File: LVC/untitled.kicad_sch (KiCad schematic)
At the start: 3 parts

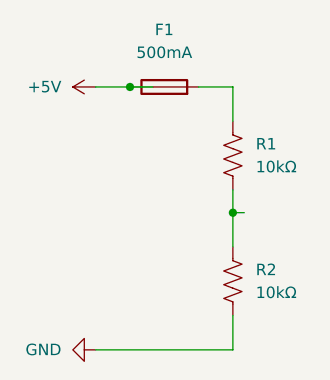
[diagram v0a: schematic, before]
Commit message: Refining Schematics
Refined the visuals of all the schematics to remove values from components. Also removed a redundant schematic.
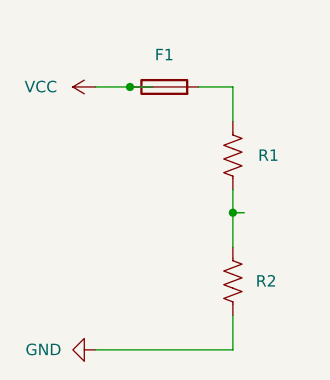
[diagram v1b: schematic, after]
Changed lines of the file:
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@@
 		(in_pos_files yes)
 		(dnp no)
-		(fields_autoplaced yes)
 		(property "Reference" "F1"
-			(at 143.51 64.77 90)
+			(at 143.51 67.564 90)
 			(show_name no)
 			(do_not_autoplace no)
@@
 		(property "Value" "500mA"
 			(at 143.51 67.31 90)
+			(hide yes)
 			(show_name no)
 			(do_not_autoplace no)
@@
 		(in_pos_files yes)
 		(dnp no)
-		(fields_autoplaced yes)
 		(property "Reference" "R2"
-			(at 153.67 91.4399 0)
+			(at 153.67 92.71 0)
 			(show_name no)
 			(do_not_autoplace no)
@@
 		(property "Value" "10kΩ"
 			(at 153.67 93.9799 0)
+			(hide yes)
 			(show_name no)
 			(do_not_autoplace no)
@@
 		(in_pos_files yes)
 		(dnp no)
-		(fields_autoplaced yes)
 		(property "Reference" "R1"
-			(at 153.67 77.4699 0)
+			(at 153.924 78.74 0)
 			(show_name no)
 			(do_not_autoplace no)
@@
 		(property "Value" "10kΩ"
 			(at 153.67 80.0099 0)
+			(hide yes)
 			(show_name no)
 			(do_not_autoplace no)
@@
 		(in_pos_files yes)
 		(dnp no)
-		(fields_autoplaced yes)
-		(property "Reference" "#PWR07"
-			(at 139.7 71.12 0)
-			(hide yes)
+		(property "Reference" "VCC"
+			(at 129.794 71.12 90)
 			(show_name no)
 			(do_not_autoplace no)
@@
 		(property "Value" "+5V"
 			(at 132.08 71.1199 90)
+			(hide yes)
 			(show_name no)
 			(do_not_autoplace no)
@@
 			(project "LVC"
 				(path "/403adfe1-51af-4c7e-94f3-ace1a53bb045"
-					(reference "#PWR07")
-					(unit 1)
-				)
+					(reference "VCC")
+					(unit 1)
+				)
